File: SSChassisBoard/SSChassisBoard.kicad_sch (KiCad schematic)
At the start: 18 parts, among them J1 Conn_01x10, J2 CONN_06SILK_FEMALE_PTH, J3 CONN_06SILK_FEMALE_PTH, J4 Conn_02x10_Odd_Even, J5 POWER, J6 Switch, M1 Left MOTOR, M2 Right MOTOR, SW1 TACT_SW, U1 DFRobot_DC_Controller

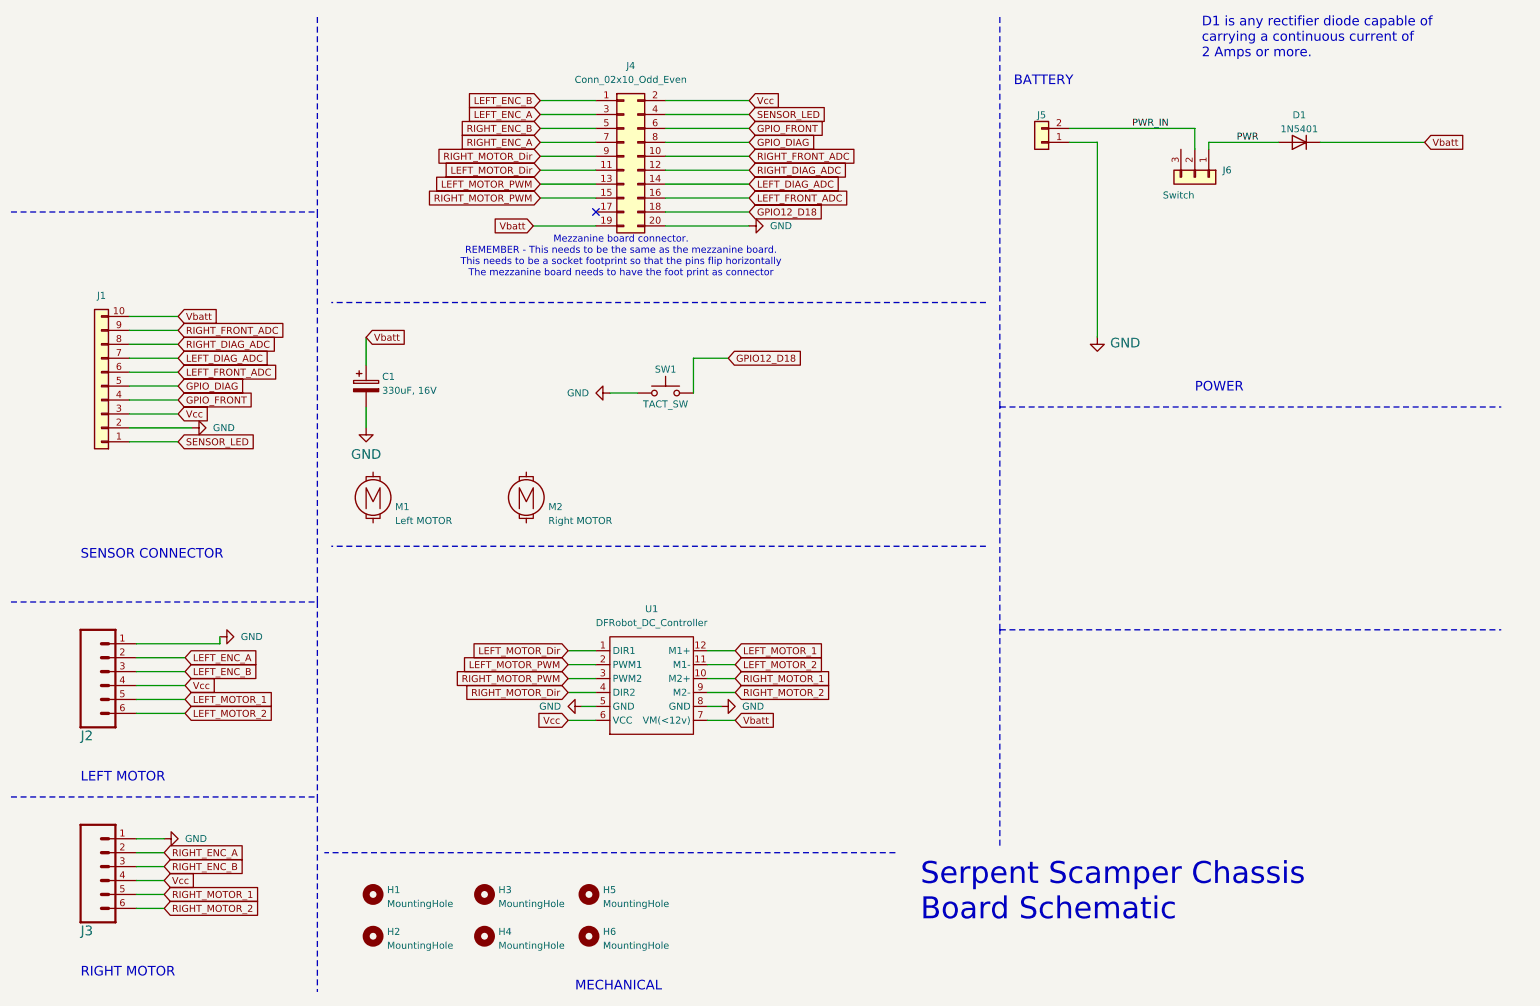
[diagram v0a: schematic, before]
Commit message: Version 2 of boards sent to JLCPCB and a new calibration board
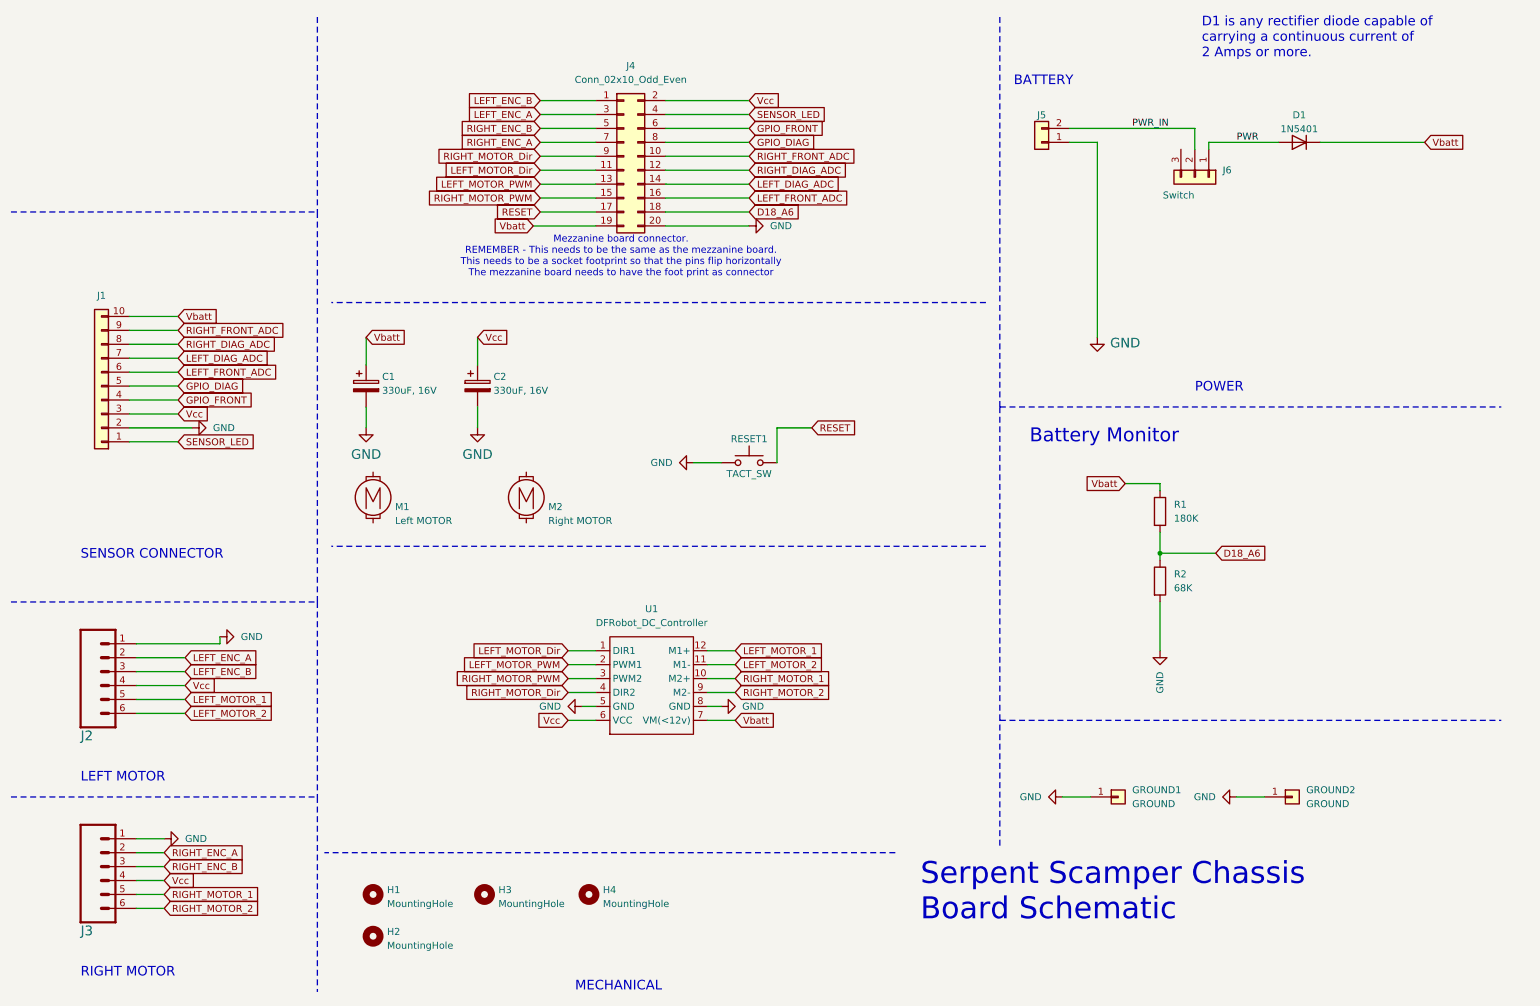
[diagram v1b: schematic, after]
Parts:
- removed H4, H6: MountingHole, ukmarsbot:MountingHole_3.2mm_M3_clearance, symbol Mechanical:MountingHole
- removed SW1: TACT_SW, Button_Switch_THT:SW_PUSH_6mm, symbol PB_Library:Tact_Switch_6mm
- added C2: 330uF, 16V, Capacitor_THT:CP_Radial_D8.0mm_P2.50mm, symbol Device:C_Polarized
- added GROUND1, GROUND2: GROUND, Connector_PinHeader_2.54mm:PinHeader_1x01_P2.54mm_Vertical, symbol Connector_Generic:Conn_01x01
- added R1: 180K, Resistor_THT:R_Axial_DIN0207_L6.3mm_D2.5mm_P7.62mm_Horizontal, symbol Device:R
- added R2: 68K, Resistor_THT:R_Axial_DIN0207_L6.3mm_D2.5mm_P7.62mm_Horizontal, symbol Device:R
- added RESET1: TACT_SW, Button_Switch_THT:SW_PUSH_6mm, symbol PB_Library:Tact_Switch_6mm
- renumbered H5 to H4
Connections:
- net GND: now also C2.2, GROUND1.1 (Pin_1), GROUND2.1 (Pin_1), R2.2, RESET1.1 (A)
- net Vbatt: now also R1.1
- net Vcc: now also C2.1
- net RESET: now reaches J4.17 (Pin_17)
- net RESET: now also RESET1.2 (B)
- net GPIO12_D18 renamed D18_A6
- net D18_A6: now also R1.2, R2.1
- no-connect marks 1 -> 0
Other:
- note added: "Battery Monitor"
